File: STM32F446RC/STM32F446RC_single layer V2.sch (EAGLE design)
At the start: 75 parts, among them IC1 STM32F446RCT6

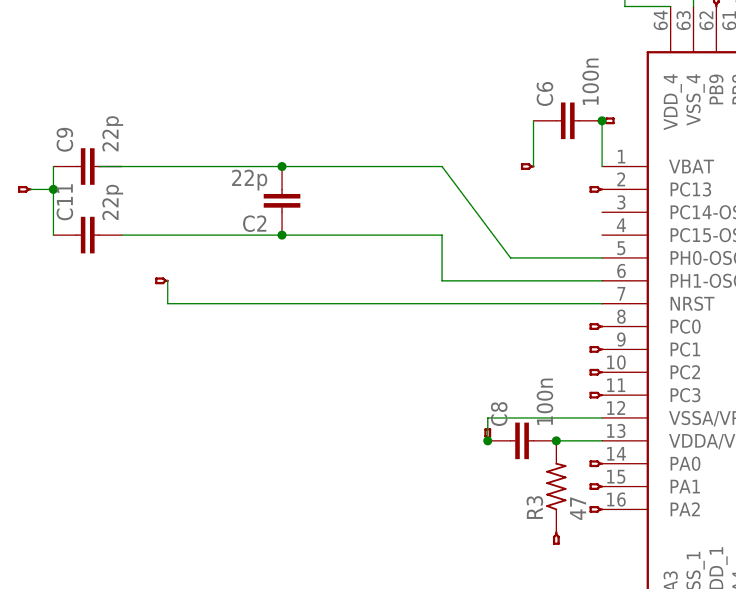
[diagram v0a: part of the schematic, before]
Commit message: added double layer
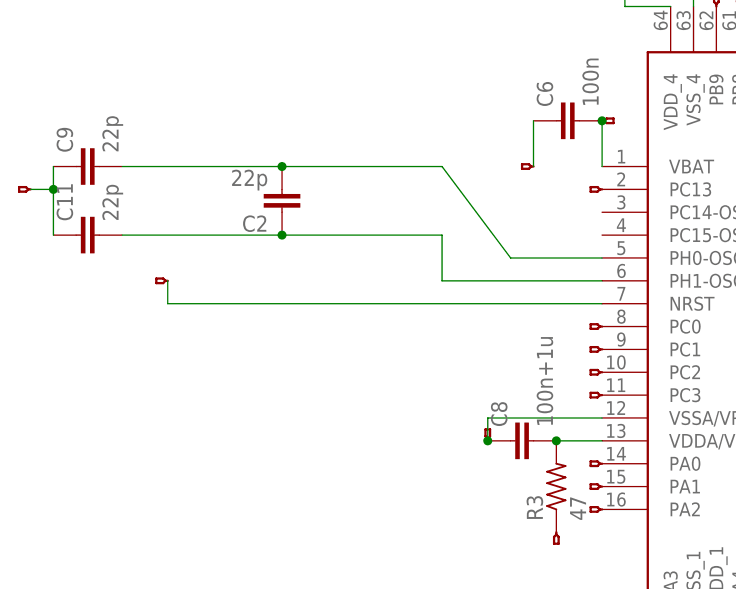
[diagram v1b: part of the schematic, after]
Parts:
- C8: value 100n -> 100n+1u
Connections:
- removed net N$53: C2.2, IC1.PH0-OSC_IN
- new net N$61: C2.2, C9.2, IC1.PH0-OSC_IN
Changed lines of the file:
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@@
 <part name="C6" library="capacitor-wima" library_urn="urn:adsk.eagle:library:116" deviceset="C" device="2,5-3" package3d_urn="urn:adsk.eagle:package:5436/1" value="100n"/>
 <part name="C7" library="capacitor-wima" library_urn="urn:adsk.eagle:library:116" deviceset="C" device="2,5-3" package3d_urn="urn:adsk.eagle:package:5436/1" value="2.2U"/>
-<part name="C8" library="capacitor-wima" library_urn="urn:adsk.eagle:library:116" deviceset="C" device="2,5-3" package3d_urn="urn:adsk.eagle:package:5436/1" value="100n"/>
+<part name="C8" library="capacitor-wima" library_urn="urn:adsk.eagle:library:116" deviceset="C" device="2,5-3" package3d_urn="urn:adsk.eagle:package:5436/1" value="100n+1u"/>
 <part name="C9" library="capacitor-wima" library_urn="urn:adsk.eagle:library:116" deviceset="C" device="2,5-3" package3d_urn="urn:adsk.eagle:package:5436/1" value="22p"/>
 <part name="C11" library="capacitor-wima" library_urn="urn:adsk.eagle:library:116" deviceset="C" device="2,5-3" package3d_urn="urn:adsk.eagle:package:5436/1" value="22p"/>
@@
 <instance part="C2" gate="G$1" x="-5.08" y="58.42" rot="R180">
 <attribute name="NAME" x="-6.604" y="58.039" size="1.778" layer="95" rot="R180"/>
-<attribute name="VALUE" x="-6.604" y="63.119" size="1.778" layer="96" rot="R180"/>
 </instance>
 </instances>
@@
 </segment>
 </net>
-<net name="N$53" class="0">
-<segment>
-<pinref part="IC1" gate="G$1" pin="PH0-OSC_IN"/>
-<wire x1="30.48" y1="53.34" x2="20.32" y2="53.34" width="0.1524" layer="91"/>
-<wire x1="20.32" y1="53.34" x2="12.7" y2="63.5" width="0.1524" layer="91"/>
-<wire x1="12.7" y1="63.5" x2="-5.08" y2="63.5" width="0.1524" layer="91"/>
-<wire x1="-5.08" y1="63.5" x2="-25.4" y2="63.5" width="0.1524" layer="91"/>
-<pinref part="C2" gate="G$1" pin="2"/>
-<junction x="-5.08" y="63.5"/>
-</segment>
-</net>
 <net name="N$54" class="0">
 <segment>
@@
 </segment>
 </net>
+<net name="N$61" class="0">
+<segment>
+<pinref part="C9" gate="G$1" pin="2"/>
+<pinref part="C2" gate="G$1" pin="2"/>
+<wire x1="-22.86" y1="63.5" x2="-5.08" y2="63.5" width="0.1524" layer="91"/>
+<pinref part="IC1" gate="G$1" pin="PH0-OSC_IN"/>
+<wire x1="30.48" y1="53.34" x2="20.32" y2="53.34" width="0.1524" layer="91"/>
+<wire x1="20.32" y1="53.34" x2="12.7" y2="63.5" width="0.1524" layer="91"/>
+<wire x1="-5.08" y1="63.5" x2="12.7" y2="63.5" width="0.1524" layer="91"/>
+<junction x="-5.08" y="63.5"/>
+</segment>
+</net>
